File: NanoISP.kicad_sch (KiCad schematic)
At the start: 12 parts, among them J1 Conn_02x03_Odd_Even

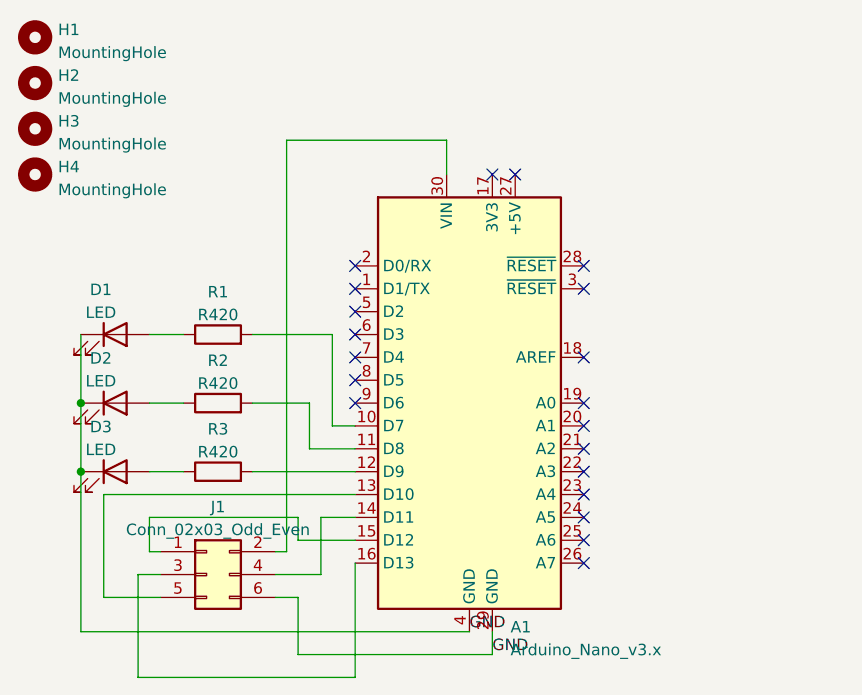
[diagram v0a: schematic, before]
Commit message: Added the capacitor for handling ready / unready.
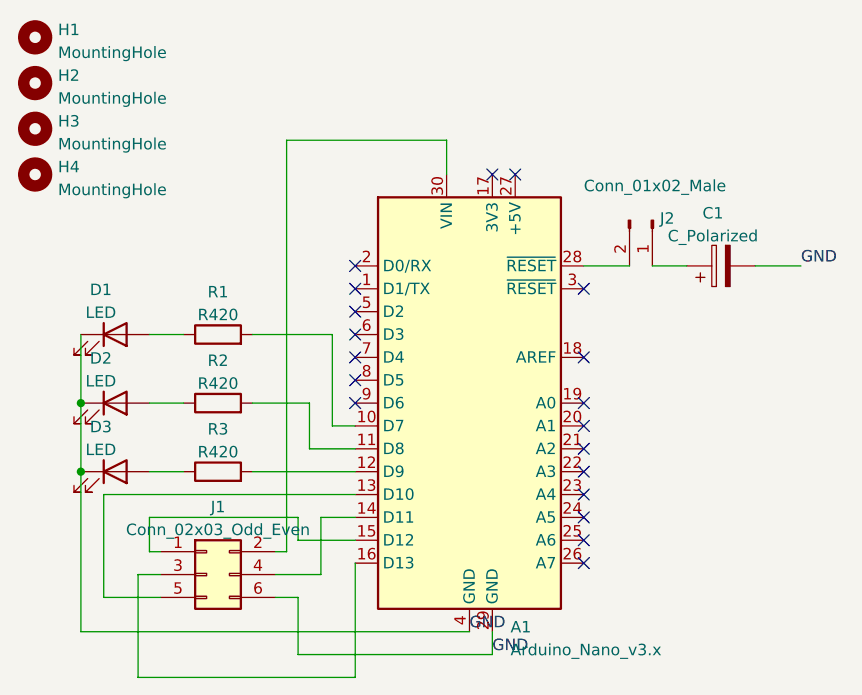
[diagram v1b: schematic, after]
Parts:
- added C1: C_Polarized, Capacitor_THT:CP_Radial_D5.0mm_P2.50mm, symbol Device:C_Polarized
- added J2: Conn_01x02_Male, Connector_PinHeader_2.54mm:PinHeader_1x02_P2.54mm_Vertical, symbol Connector:Conn_01x02_Male
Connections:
- net GND: now also C1.2
- net at A1.28 (~{RESET}): now also J2.2 (Pin_2)
- new net: C1.1, J2.1 (Pin_1)
- no-connect marks 20 -> 19
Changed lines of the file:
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@@
   (no_connect (at 76.2 38.1))
   (no_connect (at 78.74 38.1))
-  (no_connect (at 86.36 48.26))
   (no_connect (at 60.96 48.26))
   (no_connect (at 60.96 50.8))
@@
     (stroke (width 0) (type default) (color 0 0 0 0))
   )
+  (wire (pts (xy 93.98 48.26) (xy 97.79 48.26))
+    (stroke (width 0) (type default) (color 0 0 0 0))
+  )
   (wire (pts (xy 55.88 63.5) (xy 49.53 63.5))
     (stroke (width 0) (type default) (color 0 0 0 0))
@@
     (stroke (width 0) (type default) (color 0 0 0 0))
   )
+  (wire (pts (xy 86.36 48.26) (xy 91.44 48.26))
+    (stroke (width 0) (type default) (color 0 0 0 0))
+  )
   (wire (pts (xy 36.83 82.55) (xy 36.83 93.98))
     (stroke (width 0) (type default) (color 0 0 0 0))
@@
     (stroke (width 0) (type default) (color 0 0 0 0))
   )
+  (wire (pts (xy 105.41 48.26) (xy 110.49 48.26))
+    (stroke (width 0) (type default) (color 0 0 0 0))
+  )
   (wire (pts (xy 38.1 55.88) (xy 41.91 55.88))
     (stroke (width 0) (type default) (color 0 0 0 0))
@@
   )
   (label "GND" (at 73.66 88.9 0)
+    (effects (font (size 1.27 1.27)) (justify left bottom))
+  )
+  (label "GND" (at 110.49 48.26 0)
     (effects (font (size 1.27 1.27)) (justify left bottom))
   )
@@
     (pin "9")
   )
+  (symbol (lib_id "Connector:Conn_01x02_Male") (at 93.98 43.18 270) (unit 1)
+    (in_bom yes) (on_board yes)
+    (property "Reference" "J2" (id 0) (at 94.8182 42.9803 90)
+      (effects (font (size 1.27 1.27)) (justify left))
+    )
+    (property "Value" "Conn_01x02_Male" (id 1) (at 86.36 39.37 90)
+      (effects (font (size 1.27 1.27)) (justify left))
+    )
+    (property "Footprint" "Connector_PinHeader_2.54mm:PinHeader_1x02_P2.54mm_Vertical" (id 2) (at 93.98 43.18 0)
+      (effects (font (size 1.27 1.27)) hide)
+    )
+    (property "Datasheet" "~" (id 3) (at 93.98 43.18 0)
+      (effects (font (size 1.27 1.27)) hide)
+    )
+    (pin "1")
+    (pin "2")
+  )
+  (symbol (lib_id "Device:C_Polarized") (at 101.6 48.26 90) (unit 1)
+    (in_bom yes) (on_board yes) (fields_autoplaced)
+    (property "Reference" "C1" (id 0) (at 100.711 42.4012 90))
+    (property "Value" "C_Polarized" (id 1) (at 100.711 44.9381 90))
+    (property "Footprint" "Capacitor_THT:CP_Radial_D5.0mm_P2.50mm" (id 2) (at 105.41 47.2948 0)
+      (effects (font (size 1.27 1.27)) hide)
+    )
+    (property "Datasheet" "~" (id 3) (at 101.6 48.26 0)
+      (effects (font (size 1.27 1.27)) hide)
+    )
+    (pin "1")
+    (pin "2")
+  )
   (symbol (lib_id "Mechanical:MountingHole") (at 25.4 27.94 0) (unit 1)
     (in_bom yes) (on_board yes) (fields_autoplaced)
@@
       (reference "A1") (unit 1) (value "Arduino_Nano_v3.x") (footprint "Module:Arduino_Nano")
     )
+    (path "/5ca76dbc-8bbb-4e44-b0c9-01dc175390ca"
+      (reference "C1") (unit 1) (value "C_Polarized") (footprint "Capacitor_THT:CP_Radial_D5.0mm_P2.50mm")
+    )
     (path "/d3060307-2c26-4d91-931e-3ca65ef351b7"
       (reference "D1") (unit 1) (value "LED") (footprint "LED_THT:LED_D5.0mm")
@@
       (reference "J1") (unit 1) (value "Conn_02x03_Odd_Even") (footprint "Connector_PinHeader_2.54mm:PinHeader_2x03_P2.54mm_Vertical")
     )
+    (path "/364e8e46-564c-408f-84de-58cf1e226072"
+      (reference "J2") (unit 1) (value "Conn_01x02_Male") (footprint "Connector_PinHeader_2.54mm:PinHeader_1x02_P2.54mm_Vertical")
+    )
     (path "/be3c1a07-d7c7-4961-a2bf-88f27591b364"

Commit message: Fixed a small bug.
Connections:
- net at A1.27 (+5V): now also J1.2 (Pin_2)
- net at A1.30 (VIN): no longer J1.2 (Pin_2)
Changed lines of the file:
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@@
   (no_connect (at 86.36 50.8))
   (no_connect (at 76.2 38.1))
-  (no_connect (at 78.74 38.1))
+  (no_connect (at 71.12 38.1))
   (no_connect (at 60.96 48.26))
   (no_connect (at 60.96 50.8))
@@
     (stroke (width 0) (type default) (color 0 0 0 0))
   )
-  (wire (pts (xy 71.12 34.29) (xy 53.34 34.29))
+  (wire (pts (xy 78.74 34.29) (xy 53.34 34.29))
     (stroke (width 0) (type default) (color 0 0 0 0))
   )
@@
     (stroke (width 0) (type default) (color 0 0 0 0))
   )
-  (wire (pts (xy 71.12 34.29) (xy 71.12 38.1))
-    (stroke (width 0) (type default) (color 0 0 0 0))
-  )
   (wire (pts (xy 57.15 76.2) (xy 60.96 76.2))
     (stroke (width 0) (type default) (color 0 0 0 0))
@@
     (stroke (width 0) (type default) (color 0 0 0 0))
   )
+  (wire (pts (xy 78.74 34.29) (xy 78.74 38.1))
+    (stroke (width 0) (type default) (color 0 0 0 0))
+  )
